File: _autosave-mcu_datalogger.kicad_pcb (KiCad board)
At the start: 2 copper layers, 50.6 x 30.6 mm, 29 parts, among them J1 Conn_01x04_Pin, J2 Conn_01x04_Pin, J3 Conn_01x09, J4 Conn_02x03_Counter_Clockwise, U1 DS1337S_, U3 24LC1025, U4 24LC1025, U5 ATMEGA328P-AU, Y1 32.768 KHz, Y2 16MHz

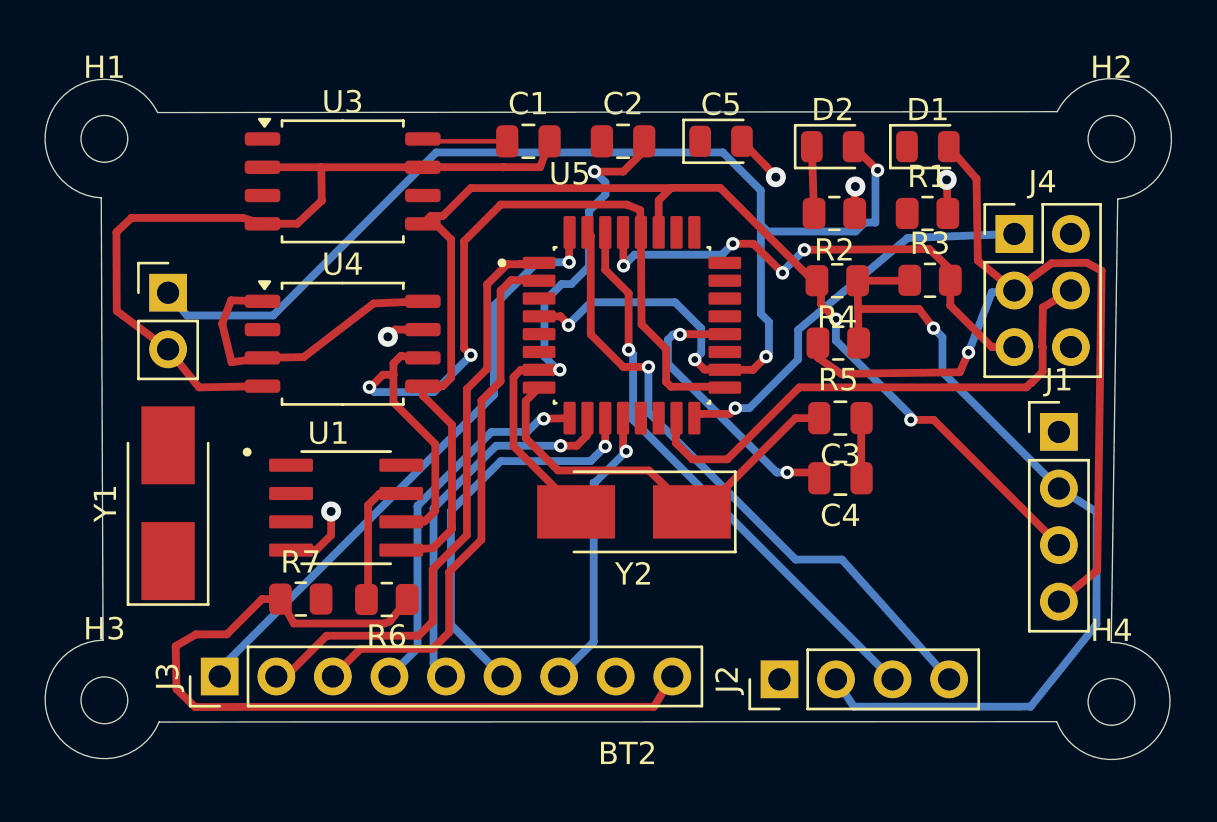
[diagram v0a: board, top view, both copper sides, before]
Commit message: Added the Zones for GND & VCC
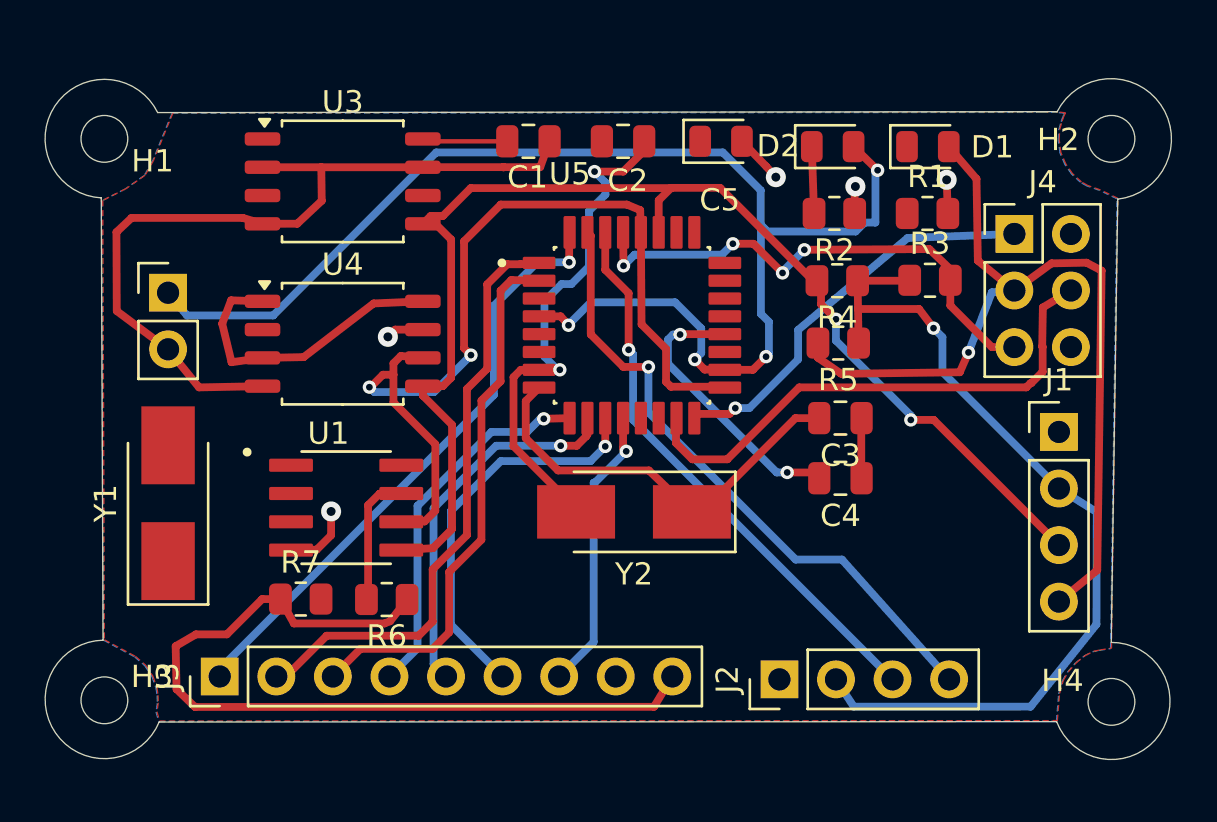
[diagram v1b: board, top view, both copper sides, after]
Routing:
- added copper zone on F.Cu, net /Vcc
- added copper zone on B.Cu, net GND
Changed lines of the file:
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@@
 			(at 0 9.95 90)
 			(layer "F.Fab")
+			(hide yes)
 			(effects
 				(font
@@
 		(tags "capacitor")
 		(property "Reference" "C1"
-			(at 0 -1.68 0)
+			(at -0.04 1.61 0)
 			(layer "F.SilkS")
 			(effects
@@
 		(tags "LED")
 		(property "Reference" "D1"
-			(at 0 -1.65 0)
+			(at 2.8925 0.02 0)
 			(layer "F.SilkS")
 			(effects
@@
 		(tags "mounting hole 2.1mm no annular")
 		(property "Reference" "H2"
-			(at 0 -3.2 0)
+			(at -2.39 0.04 0)
 			(layer "F.SilkS")
 			(effects
@@
 			(at 0 3.2 0)
 			(layer "F.Fab")
+			(hide yes)
 			(effects
 				(font
@@
 		(tags "capacitor")
 		(property "Reference" "C2"
-			(at 0 -1.68 0)
+			(at 0.21 1.76 0)
 			(layer "F.SilkS")
 			(effects
@@
 		(tags "mounting hole 2.1mm no annular")
 		(property "Reference" "H1"
-			(at 0 -3.2 0)
+			(at 2.16 1 0)
 			(layer "F.SilkS")
 			(effects
@@
 			(at 0 3.2 0)
 			(layer "F.Fab")
+			(hide yes)
 			(effects
 				(font
@@
 			(at 0 22.65 90)
 			(layer "F.Fab")
+			(hide yes)
 			(effects
 				(font
@@
 			(at 1.27 7.41 0)
 			(layer "F.Fab")
+			(hide yes)
 			(effects
 				(font
@@
 		(tags "mounting hole 2.1mm no annular")
 		(property "Reference" "H3"
-			(at 0 -3.2 0)
+			(at 2.14 -1.06 0)
 			(layer "F.SilkS")
 			(effects
@@
 			(at 0 3.2 0)
 			(layer "F.Fab")
+			(hide yes)
 			(effects
 				(font
@@
 		(tags "LED")
 		(property "Reference" "C5"
-			(at 0 -1.65 0)
+			(at -0.06 2.64 0)
 			(layer "F.SilkS")
 			(effects
@@
 		(tags "Through hole pin header THT 1x02 2.54mm single row")
 		(property "Reference" "BT2"
-			(at 20.63 20.7 0)
+			(at 0.07 -2.42 0)
 			(layer "F.SilkS")
+			(hide yes)
 			(effects
 				(font
@@
 		(tags "mounting hole 2.1mm no annular")
 		(property "Reference" "H4"
-			(at 0 -3.2 0)
+			(at -2.2 -0.95 0)
 			(layer "F.SilkS")
 			(effects
@@
 		)
 		(property "Value" "MountingHole"
-			(at 0 3.2 0)
+			(at -2.83 6.47 0)
 			(layer "F.Fab")
+			(hide yes)
 			(effects
 				(font
@@
 		(tags "LED")
 		(property "Reference" "D2"
-			(at 0 -1.65 0)
+			(at -2.4525 -0.03 0)
 			(layer "F.SilkS")
 			(effects
@@
 		(net 36)
 	)
+	(zone
+		(net 9)
+		(net_name "/Vcc")
+		(layer "F.Cu")
+		(hatch edge 0.5)
+		(connect_pads
+			(clearance 0.5)
+		)
+		(min_thickness 0.25)
+		(filled_areas_thickness no)
+		(fill
+			(mode hatch)
+			(thermal_gap 0.5)
+			(thermal_bridge_width 0.5)
+			(hatch_thickness 1)
+			(hatch_gap 1.5)
+			(hatch_orientation 0)
+			(hatch_border_algorithm hatch_thickness)
+			(hatch_min_hole_area 0.3)
+		)
+		(polygon
+			(pts
+				(xy 224.279925 65.521454) (xy 185.219925 65.561454) (xy 184.339925 67.711454) (xy 183.969925 68.361454)
+				(xy 183.119925 68.961454) (xy 182.069925 69.491454) (xy 182.139925 89.221454) (xy 183.539925 89.971454)
+				(xy 183.999925 90.371454) (xy 184.319925 90.861454) (xy 184.499925 91.371454) (xy 184.549925 91.711454)
+				(xy 184.559925 92.051454) (xy 184.499925 92.451454) (xy 184.619925 92.871454) (xy 224.929925 92.851454)
+				(xy 225.029925 91.631454) (xy 225.199925 91.041454) (xy 225.419925 90.661454) (xy 225.769925 90.261454)
+				(xy 226.179925 89.931454) (xy 226.549925 89.741454) (xy 226.839925 89.681454) (xy 227.359925 89.601454)
+				(xy 227.649925 69.401454) (xy 226.859925 69.021454) (xy 226.289925 68.821454) (xy 226.009925 68.661454)
+				(xy 225.609925 68.291454) (xy 225.309925 67.861454) (xy 225.089925 67.351454) (xy 225.009925 66.751454)
+				(xy 225.039925 66.291454) (xy 225.139925 65.941454) (xy 225.229925 65.691454) (xy 225.299925 65.561454)
+				(xy 224.959925 65.521454)
+			)
+		)
+	)
+	(zone
+		(net 1)
+		(net_name "GND")
+		(layer "B.Cu")
+		(hatch edge 0.5)
+		(connect_pads
+			(clearance 0.5)
+		)
+		(min_thickness 0.25)
+		(filled_areas_thickness no)
+		(fill
+			(mode hatch)
+			(thermal_gap 0.5)
+			(thermal_bridge_width 0.5)
+			(hatch_thickness 1)
+			(hatch_gap 1.5)
+			(hatch_orientation 0)
+			(hatch_border_algorithm hatch_thickness)
+			(hatch_min_hole_area 0.3)
+		)
+		(polygon
+			(pts
+				(xy 224.24 65.54) (xy 185.18 65.58) (xy 184.3 67.73) (xy 183.93 68.38) (xy 183.08 68.98) (xy 182.03 69.51)
+				(xy 182.1 89.24) (xy 183.5 89.99) (xy 183.96 90.39) (xy 184.28 90.88) (xy 184.46 91.39) (xy 184.51 91.73)
+				(xy 184.52 92.07) (xy 184.46 92.47) (xy 184.58 92.89) (xy 224.89 92.87) (xy 224.99 91.65) (xy 225.16 91.06)
+				(xy 225.38 90.68) (xy 225.73 90.28) (xy 226.14 89.95) (xy 226.51 89.76) (xy 226.8 89.7) (xy 227.32 89.62)
+				(xy 227.61 69.42) (xy 226.82 69.04) (xy 226.25 68.84) (xy 225.97 68.68) (xy 225.57 68.31) (xy 225.27 67.88)
+				(xy 225.05 67.37) (xy 224.97 66.77) (xy 225 66.31) (xy 225.1 65.96) (xy 225.19 65.71) (xy 225.26 65.58)
+				(xy 224.92 65.54)
+			)
+		)
+	)
 )

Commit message: Add board hardware image and update README
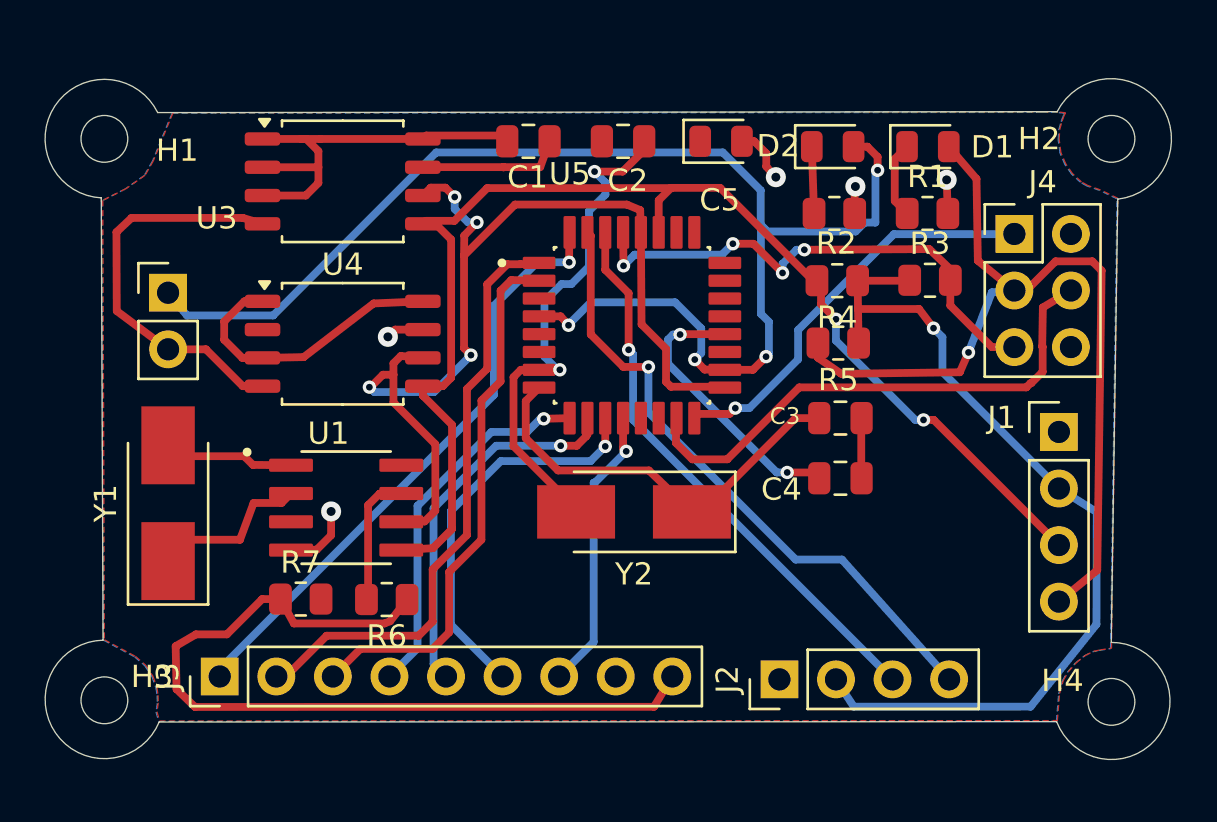
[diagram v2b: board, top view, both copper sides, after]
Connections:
- net Net-(D1-K) renamed /R1_1
- net Net-(U1-X1) renamed /X1
- net Net-(U1-X2) renamed /X2
- BT2 pad 1: Net-(BT2-+) -> /AVCC
- C5 pad 1: Net-(BT2-+) -> /AVCC
- D1 pad 2: Net-(BT2-+) -> /AVCC
- D2 pad 2: Net-(BT2-+) -> /SCK
- J4 pad 2: /Vcc -> /SCK
- J4 pad 3: /SCK -> /RESET
- J4 pad 4: /MOSI -> GND
- J4 pad 5: /RESET -> /MOSI
- U5 pad 18: Net-(BT2-+) -> /AVCC
- U5 pad 4: Net-(BT2-+) -> /AVCC
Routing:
- net /SCK: track 82.6 -> 150.2 mm, vias 3 -> 9
- net Net-(BT2-+): track 62.1 -> 0.00 mm, vias 4 -> 0
- net /Vcc: track 95.0 -> 109.3 mm
- net GND: track 49.2 -> 37.7 mm
- net /X2: track 0.00 -> 7.24 mm
- net /X1: track 0.00 -> 5.88 mm
- net /R1_1: track 0.00 -> 3.46 mm
